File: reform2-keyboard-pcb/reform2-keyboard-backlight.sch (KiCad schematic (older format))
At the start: 94 parts, among them U2 TPS61185

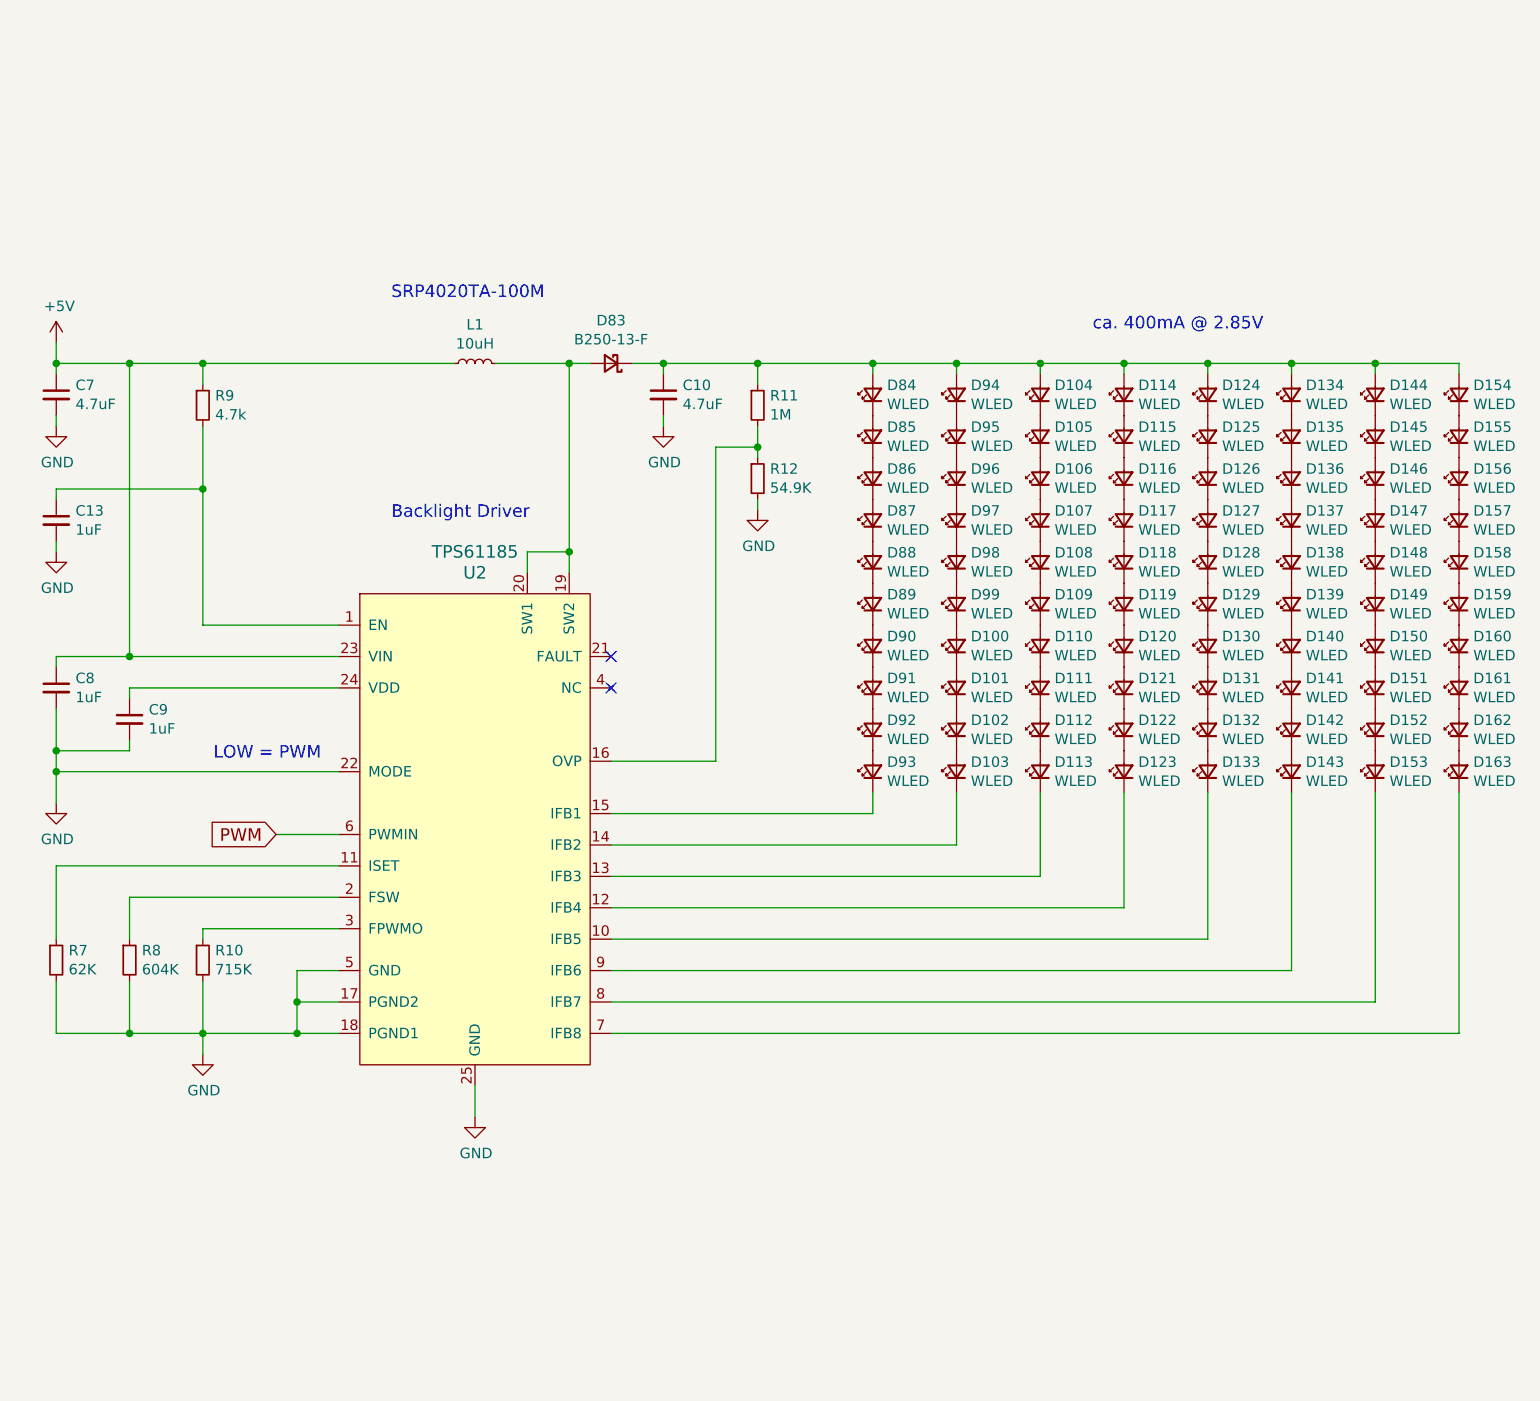
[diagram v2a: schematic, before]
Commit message: keyboard: add WIP R-2D version, atmega RC notes
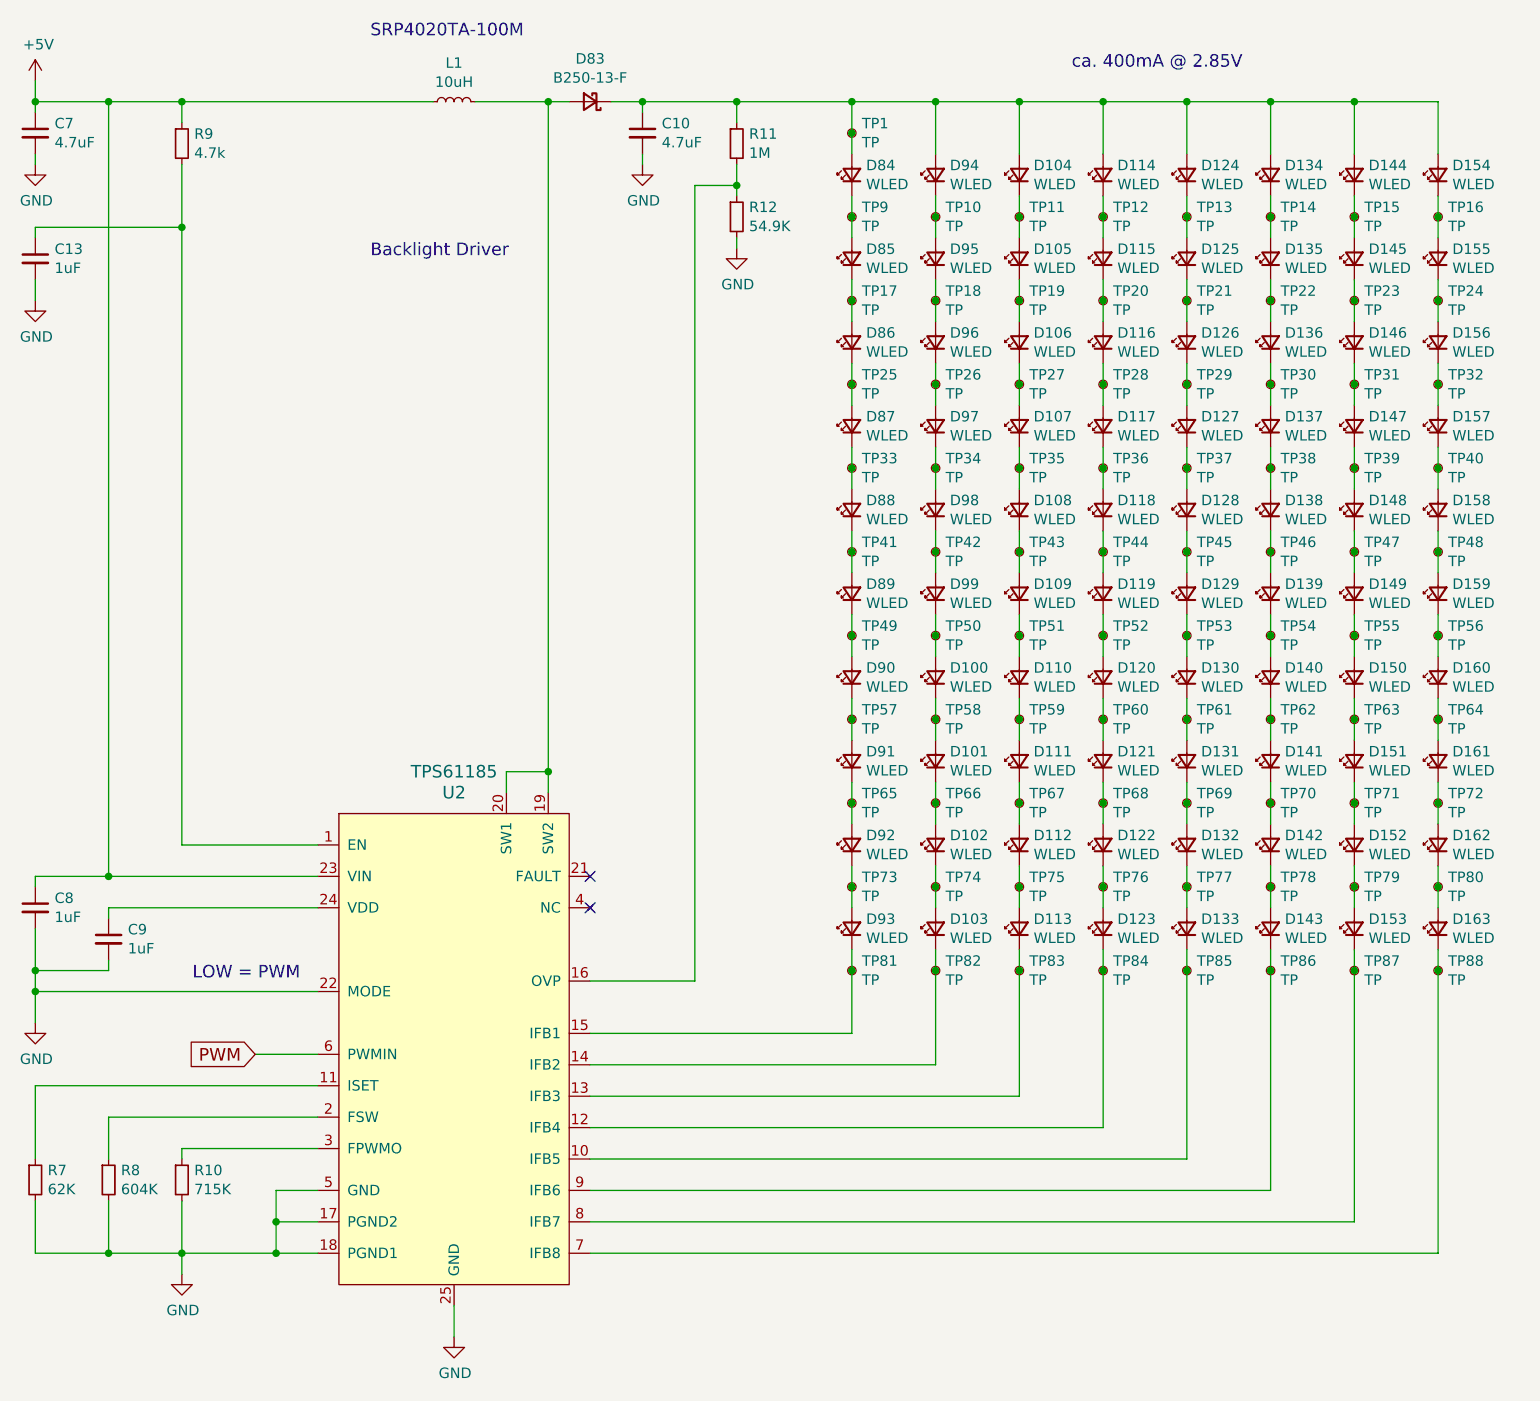
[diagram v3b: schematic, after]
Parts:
- added TP1, TP10, TP11, TP12, TP13, TP14, TP15, TP16, TP17, TP18, TP19, TP20, TP21, TP22, TP23, TP24, TP25, TP26, TP27, TP28, TP29, TP30, TP31, TP32, TP33, TP34, TP35, TP36, TP37, TP38, TP39, TP40, TP41, TP42, TP43, TP44, TP45, TP46, TP47, TP48, TP49, TP50, TP51, TP52, TP53, TP54, TP55, TP56, TP57, TP58, TP59, TP60, TP61, TP62, TP63, TP64, TP65, TP66, TP67, TP68, TP69, TP70, TP71, TP72, TP73, TP74, TP75, TP76, TP77, TP78, TP79, TP80, TP81, TP82, TP83, TP84, TP85, TP86, TP87, TP88, TP9: TP, TestPoint:TestPoint_Pad_1.0x1.0mm, symbol Connector:TestPoint_Small
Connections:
- net at D133.1 (K), U2.10 (IFB5): now also TP85.1
- net at D123.1 (K), U2.12 (IFB4): now also TP84.1
- net at D113.1 (K), U2.13 (IFB3): now also TP83.1
- net at D103.1 (K), U2.14 (IFB2): now also TP82.1
- net at D93.1 (K), U2.15 (IFB1): now also TP81.1
- net at D163.1 (K), U2.7 (IFB8): now also TP88.1
- net at D153.1 (K), U2.8 (IFB7): now also TP87.1
- net at D143.1 (K), U2.9 (IFB6): now also TP86.1
- net at C10.1, D104.2 (A), D114.2 (A)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: now also TP1.1
- net at D84.1 (K), D85.2 (A): now also TP9.1
- net at D85.1 (K), D86.2 (A): now also TP17.1
- net at D86.1 (K), D87.2 (A): now also TP25.1
- net at D87.1 (K), D88.2 (A): now also TP33.1
- net at D88.1 (K), D89.2 (A): now also TP41.1
- net at D89.1 (K), D90.2 (A): now also TP49.1
- net at D90.1 (K), D91.2 (A): now also TP57.1
- net at D91.1 (K), D92.2 (A): now also TP65.1
- net at D94.1 (K), D95.2 (A): now also TP10.1
- net at D95.1 (K), D96.2 (A): now also TP18.1
- net at D96.1 (K), D97.2 (A): now also TP26.1
- net at D97.1 (K), D98.2 (A): now also TP34.1
- net at D98.1 (K), D99.2 (A): now also TP42.1
- net at D100.2 (A), D99.1 (K): now also TP50.1
- net at D100.1 (K), D101.2 (A): now also TP58.1
- net at D101.1 (K), D102.2 (A): now also TP66.1
- net at D104.1 (K), D105.2 (A): now also TP11.1
- net at D105.1 (K), D106.2 (A): now also TP19.1
- net at D106.1 (K), D107.2 (A): now also TP27.1
- net at D107.1 (K), D108.2 (A): now also TP35.1
- net at D108.1 (K), D109.2 (A): now also TP43.1
- net at D109.1 (K), D110.2 (A): now also TP51.1
- net at D110.1 (K), D111.2 (A): now also TP59.1
- net at D111.1 (K), D112.2 (A): now also TP67.1
- net at D114.1 (K), D115.2 (A): now also TP12.1
- net at D115.1 (K), D116.2 (A): now also TP20.1
- net at D116.1 (K), D117.2 (A): now also TP28.1
- net at D117.1 (K), D118.2 (A): now also TP36.1
- net at D118.1 (K), D119.2 (A): now also TP44.1
- net at D119.1 (K), D120.2 (A): now also TP52.1
- net at D120.1 (K), D121.2 (A): now also TP60.1
- net at D121.1 (K), D122.2 (A): now also TP68.1
- net at D124.1 (K), D125.2 (A): now also TP13.1
- net at D125.1 (K), D126.2 (A): now also TP21.1
- net at D126.1 (K), D127.2 (A): now also TP29.1
- net at D127.1 (K), D128.2 (A): now also TP37.1
- net at D128.1 (K), D129.2 (A): now also TP45.1
- net at D129.1 (K), D130.2 (A): now also TP53.1
- net at D130.1 (K), D131.2 (A): now also TP61.1
- net at D131.1 (K), D132.2 (A): now also TP69.1
- net at D134.1 (K), D135.2 (A): now also TP14.1
- net at D135.1 (K), D136.2 (A): now also TP22.1
- net at D136.1 (K), D137.2 (A): now also TP30.1
- net at D137.1 (K), D138.2 (A): now also TP38.1
- net at D138.1 (K), D139.2 (A): now also TP46.1
- net at D139.1 (K), D140.2 (A): now also TP54.1
- net at D140.1 (K), D141.2 (A): now also TP62.1
- net at D141.1 (K), D142.2 (A): now also TP70.1
- net at D144.1 (K), D145.2 (A): now also TP15.1
- net at D145.1 (K), D146.2 (A): now also TP23.1
- net at D146.1 (K), D147.2 (A): now also TP31.1
- net at D147.1 (K), D148.2 (A): now also TP39.1
- net at D148.1 (K), D149.2 (A): now also TP47.1
- net at D149.1 (K), D150.2 (A): now also TP55.1
- net at D150.1 (K), D151.2 (A): now also TP63.1
- net at D151.1 (K), D152.2 (A): now also TP71.1
- net at D154.1 (K), D155.2 (A): now also TP16.1
- net at D155.1 (K), D156.2 (A): now also TP24.1
- net at D156.1 (K), D157.2 (A): now also TP32.1
- net at D157.1 (K), D158.2 (A): now also TP40.1
- net at D158.1 (K), D159.2 (A): now also TP48.1
- net at D159.1 (K), D160.2 (A): now also TP56.1
- net at D160.1 (K), D161.2 (A): now also TP64.1
- net at D161.1 (K), D162.2 (A): now also TP72.1
- net at D92.1 (K), D93.2 (A): now also TP73.1
- net at D102.1 (K), D103.2 (A): now also TP74.1
- net at D112.1 (K), D113.2 (A): now also TP75.1
- net at D122.1 (K), D123.2 (A): now also TP76.1
- net at D132.1 (K), D133.2 (A): now also TP77.1
- net at D142.1 (K), D143.2 (A): now also TP78.1
- net at D152.1 (K), D153.2 (A): now also TP79.1
- net at D162.1 (K), D163.2 (A): now also TP80.1
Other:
- moved on the sheet: C10, C13, C7, C8, C9, D100, D101, D102, D103, D104, D105, D106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
